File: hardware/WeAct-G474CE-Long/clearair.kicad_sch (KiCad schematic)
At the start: 36 parts, among them J1 220VAC mains in, M1 AC vent fan, M2 40mm fan (5V or 12V), Q1 2N7000, Q2 2N7000, Q3 2N2222A, Q4 IRFZ44N, SW1 RESET, SW2 COLD_BOOT, U1 SPS30, U2 BME680, U3 MQ131, U4 MiCS-4514, U5 RobotDyn AC dimmer

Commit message: encloser and buzzer
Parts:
- removed Q4: IRFZ44N, Package_TO_SOT_THT:TO-220-3_Vertical, symbol Transistor_FET:IRLZ44N
- removed R16: 10k, symbol Device:R
- added Q5: AO3400A, Package_TO_SOT_SMD:SOT-23, symbol Transistor_FET:AO3400A
- added R17: 100, symbol Device:R
- added R18: 100k, symbol Device:R
- added U6: PCF8563 RTC, libraries:PCF8563_HW689, symbol FullModules:PCF8563_HW689
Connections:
- net +3V3: now also U6.1 (VCC)
- net GND: now also U4.5 (PRE), Q5.2 (S), R18.2, U6.2 (GND); no longer U3.2 (GND)
- net at A.10 (PA15), R1.2, U1.3 (SCL)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: now also U6.4 (SCL)
- net at A.3 (PB7), R2.2, U1.2 (SDA)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: now also U6.3 (SDA)
- net at A.20 (PB12): now also R17.1; no longer U4.5 (PRE)
- net at Q3.3 (C): now also BZ1.2 (-)
- new net: Q5.1 (G), R17.2, R18.1
- new net: Q5.3 (D), U3.2 (GND)
- no-connect marks 53 -> 55
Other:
- note added: "Buzzer: PB15 (BUZZER_IN) -> R9 1k -> Q3 2N2222A base. Q3 switches the 12V buzzer on its low side: PB15 HIGH -> buzzer ON, LOW -> OFF. MiCS-4514 PRE tied to GND (boost not used). PB12 (MQ131_PREHEAT) -> R17 100R -> Q5 AO3400A gate, R18 100k pull-down: low-side switch in the MQ131 GND, HIGH = heater on. Cold/warm boot button SW2 -> PB14 (BOOT_MODE, pull-up). Gate PB1 (TRIAC_DIMMER) -> RobotDyn PSM."
- note added: "I2C1: PA15 SCL / PB7 SDA. SPS30 SEL=GND (I2C, 0x69); BME680 SDO=3V3 (0x77), CS=3V3; PCF8563 RTC HW-689 (0x51, CR1220, COT and INT unused). 4k7 pull-ups to 3V3."
- note removed: "Buzzer: PB15 (BUZZER_IN) -> R9 -> Q3. Q3 inverts: PB15 HIGH -> buzzer OFF; LOW -> R16 pulls IRFZ44N gate to 12V -> buzzer ON. MiCS-4514 PRE <- PB12 (MICS_PREHEAT). Cold/warm boot button SW2 -> PB14 (BOOT_MODE, pull-up). Gate PB1 (TRIAC_DIMMER) -> RobotDyn PSM."
- note removed: "I2C1: PA15 SCL / PB7 SDA. SPS30 SEL=GND (I2C, 0x69); BME680 SDO=3V3 (0x77), CS=3V3. 4k7 pull-ups to 3V3."

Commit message: try to make a pcb with 3D printer but the printer is dead.
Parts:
- removed JP1: FAN_V_SEL, symbol Jumper:Jumper_3_Open
- removed M2: 40mm fan (5V or 12V), symbol Motor:Fan
- removed Q5: AO3400A, Package_TO_SOT_SMD:SOT-23, symbol Transistor_FET:AO3400A
- removed R17: 100, symbol Device:R
- removed R18: 100k, symbol Device:R
- removed U1: SPS30, libraries:SPS30, symbol FullModules:SPS30
- removed U2: BME680, libraries:BME680_Board, symbol FullModules:BME680_Board
- removed U3: MQ131, libraries:MQ131_FlyingFish, symbol FullModules:MQ131_FlyingFish
- removed U4: MiCS-4514, libraries:MICS4514_Module, symbol FullModules:MICS4514_Module
- removed U6: PCF8563 RTC, libraries:PCF8563_HW689, symbol FullModules:PCF8563_HW689
- added J3: SPS30 wire header (1 VDD, 2 SDA, 3 SCL, 4 SEL, 5 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, Connector_PinHeader_2.54mm:PinHeader_1x05_P2.54mm_Vertical, symbol Connector_Generic:Conn_01x05
- added J4: BME680 wire header (1 VCC, 2 GND, 3 SCL, 4 SDA, 5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, Connector_PinHeader_2.54mm:PinHeader_1x06_P2.54mm_Vertical, symbol Connector_Generic:Conn_01x06
- added J5: MQ131 wire header (1 VCC, 2 GND, 3 DO nc, 4 AO), Connector_PinHeader_2.54mm:PinHeader_1x04_P2.54mm_Vertical, symbol Connector_Generic:Conn_01x04
- added J6: MiCS-4514 wire header (1 VCC, 2 GND, 3 RED, 4 NOX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, Connector_PinHeader_2.54mm:PinHeader_1x05_P2.54mm_Vertical, symbol Connector_Generic:Conn_01x05
- added J7: RTC PCF8563, Connector_PinHeader_2.54mm:PinHeader_1x04_P2.54mm_Vertical, symbol Connector_Generic:Conn_01x04
- added M2: 80mm fan front, Connector_PinHeader_2.54mm:PinHeader_1x04_P2.54mm_Vertical, symbol Connector_Generic:Conn_01x04
- added M3: 80mm fan rear, Connector_PinHeader_2.54mm:PinHeader_1x04_P2.54mm_Vertical, symbol Connector_Generic:Conn_01x04
- added R19, R20: 1k, Resistor_THT:R_Axial_DIN0207_L6.3mm_D2.5mm_P7.62mm_Horizontal, symbol Device:R
- added R21, R22: 10k, Resistor_THT:R_Axial_DIN0207_L6.3mm_D2.5mm_P7.62mm_Horizontal, symbol Device:R
- BZ1: footprint (none) -> Connector_PinHeader_2.54mm:PinHeader_1x02_P2.54mm_Vertical
- J1, M1: footprint (none) -> TerminalBlock_Phoenix:TerminalBlock_Phoenix_MKDS-1,5-2-5.08_1x02_P5.08mm_Horizontal
- J2: renamed from J; footprint (none) -> Connector_PinHeader_1.27mm:PinHeader_2x07_P1.27mm_Vertical
- PS1: value AC-DC PSU 220VAC -> 12V / 5V -> AC-DC PSUs 12V 2A + 5V 2A (DC out); footprint (none) -> libraries:PSU_DC_12V_5V_Inputs
- Q1, Q2, Q3: footprint Package_TO_SOT_THT:TO-92_Inline -> Package_TO_SOT_THT:TO-92_Inline_Wide
- R1, R10, R11, R12, R13, R14, R15, R2, R3, R4, R5, R6, R7, R8, R9: footprint (none) -> Resistor_THT:R_Axial_DIN0207_L6.3mm_D2.5mm_P7.62mm_Horizontal
- SW1, SW2: footprint (none) -> Button_Switch_THT:SW_PUSH_6mm
- U5: footprint (none) -> libraries:RobotDyn_Dimmer_Logic
- renumbered A to A1
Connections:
- net +12V: now also M2.2 (Pin_2), M3.2 (Pin_2)
- net +3V3: now also J4.1 (Pin_1), J4.5 (Pin_5), J4.6 (Pin_6), J7.1 (Pin_1), R21.1, R22.1
- net +5V: now also J3.1 (Pin_1), J5.1 (Pin_1), J6.1 (Pin_1)
- net GND: now also J3.4 (Pin_4), J3.5 (Pin_5), J4.2 (Pin_2), J5.2 (Pin_2), J6.2 (Pin_2), J6.5 (Pin_5), J7.2 (Pin_2), M2.1 (Pin_1), M3.1 (Pin_1)
- net at A1.10 (PA15), R1.2: now also J3.3 (Pin_3), J4.3 (Pin_3), J7.4 (Pin_4)
- net at A1.3 (PB7), R2.2: now also J3.2 (Pin_2), J4.4 (Pin_4), J7.3 (Pin_3)
- net at R7.1: now also J6.4 (Pin_4)
- net at R5.2: now also J6.3 (Pin_3)
- net at A1.14 (PA9): now also R20.2
- net at A1.15 (PA8): now also R19.2
- net at A1.30 (PA5): now also M2.3 (Pin_3), R21.2
- net at A1.7 (PB3): now also M3.3 (Pin_3), R22.2
- net at R3.1: now also J5.4 (Pin_4)
- new net: M3.4 (Pin_4), R20.1
- new net: M2.4 (Pin_4), R19.1
- no-connect marks 55 -> 50
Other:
- note added: "220VAC mains split: J1 -> RobotDyn TRIAC (fan) and two separate AC-DC supplies (12V 2A: buzzer + M2/M3 fans, 5V 2A: board + peripherals). Off board (on_board no): J1, M1 and the AC side of PS1 and U5, wired with 1.5 mm2 copper. The sensor modules (SPS30, BME680, MQ131, MiCS-4514) are off the PCB and are connected with wires to the PCB wire headers J3 (SPS30), J4 (BME680), J5 (MQ131) and J6 (MiCS-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"
- note added: "Buzzer: PB15 (BUZZER_IN) -> R9 1k -> Q3 2N2222A base. Q3 switches the 12V buzzer on its low side: PB15 HIGH -> buzzer ON, LOW -> OFF. MiCS-4514 PRE tied to GND (boost not used). MQ131 heater runs on a steady 5 V (VCC/GND straight to the rails, no switch); PB12 is unused. Cold/warm boot button SW2 -> PB14 (BOOT_MODE, pull-up). Gate PB1 (TRIAC_DIMMER) -> RobotDyn PSM."
- note added: "I2C1: PA15 SCL / PB7 SDA. SPS30 SEL=GND (I2C, 0x69); BME680 SDO=3V3 (0x77), CS=3V3; PCF8563 RTC HW-689 off-board on header J7 (VCC, GND, SDA, SCL; 0x51, CR1220, COT and INT unused). 4k7 pull-ups to 3V3."
- note removed: "220VAC mains split: J1 -> RobotDyn TRIAC (fan) and PS1 AC-DC (12V buzzer, 5V board + peripherals). PS1 pins: 1 L, 2 N, 3 +12V, 4 +5V, 5 GND. M2 40mm fan runs all the time. JP1: bridge 1-2 for a 5V fan, 2-3 for a 12V fan."
- note removed: "Buzzer: PB15 (BUZZER_IN) -> R9 1k -> Q3 2N2222A base. Q3 switches the 12V buzzer on its low side: PB15 HIGH -> buzzer ON, LOW -> OFF. MiCS-4514 PRE tied to GND (boost not used). PB12 (MQ131_PREHEAT) -> R17 100R -> Q5 AO3400A gate, R18 100k pull-down: low-side switch in the MQ131 GND, HIGH = heater on. Cold/warm boot button SW2 -> PB14 (BOOT_MODE, pull-up). Gate PB1 (TRIAC_DIMMER) -> RobotDyn PSM."
- note removed: "I2C1: PA15 SCL / PB7 SDA. SPS30 SEL=GND (I2C, 0x69); BME680 SDO=3V3 (0x77), CS=3V3; PCF8563 RTC HW-689 (0x51, CR1220, COT and INT unused). 4k7 pull-ups to 3V3."

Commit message: fix layout and script generators
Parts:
- J3: value SPS30 wire header (1 VDD, 2 SDA, 3 SCL, 4 SEL, 5 GND) -> SPS30
- J4: value BME680 wire header (1 VCC, 2 GND, 3 SCL, 4 SDA, 5 SDO, 6 CS) -> BME680
- J5: value MQ131 wire header (1 VCC, 2 GND, 3 DO nc, 4 AO) -> MQ131
- J6: value MiCS-4514 wire header (1 VCC, 2 GND, 3 RED, 4 NOX, 5 PRE) -> MiCS-4514
- SW1: value RESET -> RESET red; footprint Button_Switch_THT:SW_PUSH_6mm -> libraries:SW_Tactile_3x6_2pin
- SW2: value COLD_BOOT -> COLD_BOOT white; footprint Button_Switch_THT:SW_PUSH_6mm -> libraries:SW_Tactile_3x6_2pin
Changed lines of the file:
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@@
 			)
 		)
-		(property "Value" "MiCS-4514 wire header (1 VCC, 2 GND, 3 RED, 4 NOX, 5 PRE)"
+		(property "Value" "MiCS-4514"
 			(at 299.72 315.15 0)
 			(show_name no)
@@
 			)
 		)
-		(property "Description" "Wire header to the off-board sensor module"
+		(property "Description" "Wire header to the off-board sensor module Pins: 1 VCC, 2 GND, 3 RED, 4 NOX, 5 PRE"
 			(at 299.72 304.8 0)
 			(hide yes)
@@
 			)
 		)
-		(property "Value" "BME680 wire header (1 VCC, 2 GND, 3 SCL, 4 SDA, 5 SDO, 6 CS)"
+		(property "Value" "BME680"
 			(at 215.9 226.25 0)
 			(show_name no)
@@
 			)
 		)
-		(property "Description" "Wire header to the off-board sensor module"
+		(property "Description" "Wire header to the off-board sensor module Pins: 1 VCC, 2 GND, 3 SCL, 4 SDA, 5 SDO, 6 CS"
 			(at 215.9 214.63 0)
 			(hide yes)
@@
 			)
 		)
-		(property "Value" "COLD_BOOT"
+		(property "Value" "COLD_BOOT white"
 			(at 256.54 240.284 0)
 			(show_name no)
@@
 			)
 		)
-		(property "Footprint" "Button_Switch_THT:SW_PUSH_6mm"
+		(property "Footprint" "libraries:SW_Tactile_3x6_2pin"
 			(at 256.54 233.68 0)
 			(hide yes)
@@
 			)
 		)
-		(property "Description" "Push button switch, generic, two pins"
+		(property "Description" "Tactile push button 6 x 3.5 x 2.5 mm, 2 legs"
 			(at 256.54 238.76 0)
 			(hide yes)
@@
 			)
 		)
-		(property "Value" "RESET"
+		(property "Value" "RESET red"
 			(at 340.36 174.244 0)
 			(show_name no)
@@
 			)
 		)
-		(property "Footprint" "Button_Switch_THT:SW_PUSH_6mm"
+		(property "Footprint" "libraries:SW_Tactile_3x6_2pin"
 			(at 340.36 167.64 0)
 			(hide yes)
@@
 			)
 		)
-		(property "Description" "Push button switch, generic, two pins"
+		(property "Description" "Tactile push button 6 x 3.5 x 2.5 mm, 2 legs"
 			(at 340.36 172.72 0)
 			(hide yes)
@@
 			)
 		)
-		(property "Value" "SPS30 wire header (1 VDD, 2 SDA, 3 SCL, 4 SEL, 5 GND)"
+		(property "Value" "SPS30"
 			(at 215.9 190.69 0)
 			(show_name no)
@@
 			)
 		)
-		(property "Description" "Wire header to the off-board sensor module"
+		(property "Description" "Wire header to the off-board sensor module Pins: 1 VDD, 2 SDA, 3 SCL, 4 SEL, 5 GND"
 			(at 215.9 180.34 0)
 			(hide yes)
@@
 			)
 		)
-		(property "Value" "MQ131 wire header (1 VCC, 2 GND, 3 DO nc, 4 AO)"
+		(property "Value" "MQ131"
 			(at 396.24 189.42 0)
 			(show_name no)
@@
 			)
 		)
-		(property "Description" "Wire header to the off-board sensor module"
+		(property "Description" "Wire header to the off-board sensor module Pins: 1 VCC, 2 GND, 3 DO nc, 4 AO"
 			(at 396.24 180.34 0)
 			(hide yes)

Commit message: fix layout and script generators
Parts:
- A1: Net NRST (none) -> Reset button; Net PA0 (none) -> MQ131 out; Net PA1 (none) -> MiCS CO; Net PA15 (none) -> I2C SCL; Net PA5 (none) -> Front fan tach; Net PA7 (none) -> MiCS NO2; Net PA8 (none) -> Front fan PWM; Net PA9 (none) -> Rear fan PWM; Net PB0 (none) -> ZC in; Net PB1 (none) -> TRIAC gate; Net PB10 (none) -> Display TX; Net PB11 (none) -> Display RX; Net PB14 (none) -> Cold-boot button; Net PB15 (none) -> Buzzer drive; Net PB3 (none) -> Rear fan tach; Net PB7 (none) -> I2C SDA; Role (none) -> mcu female
- BZ1: Net - (none) -> Buzzer GND; Role (none) -> heavy
- J3: Role (none) -> sensor
- J5: Net Pin_4 (none) -> MQ131 out; Role (none) -> sensor
- J6: Net Pin_3 (none) -> MiCS CO; Net Pin_4 (none) -> MiCS NO2; Role (none) -> sensor
- M1: Role (none) -> heavy
- M2: Net Pin_4 (none) -> Front fan PWM; Role (none) -> heavy
- M3: Net Pin_4 (none) -> Rear fan PWM; Role (none) -> heavy
- PS1: Role (none) -> post heavy
- Q1: Net D (none) -> Display TX
- Q2: Net D (none) -> Display RX
- Q3: Net B (none) -> Buzzer base
- U5: Net Z-C (none) -> ZC out; Role (none) -> header

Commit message: crate a wire buses for power
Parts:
- R1, R2: Role (none) -> bus
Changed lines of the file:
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@@
+			)
+		)
+		(property "Role" "bus"
+			(at 248.92 144.78 0)
+			(hide yes)
+			(show_name no)
+			(do_not_autoplace no)
+			(effects
+				(font
+					(size 1.27 1.27)
+				)
 			)
 		)
@@
 			(at 259.08 144.78 0)
 			(hide yes)
+			(show_name no)
+			(do_not_autoplace no)
+			(effects
+				(font
+					(size 1.27 1.27)
+				)
+			)
+		)
+		(property "Role" "bus"
+			(at 259.08 144.78 0)
+			(hide yes)

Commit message: move buees on B1
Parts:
- R1, R2: Bus area (none) -> A14:Q18
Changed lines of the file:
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@@
+			)
+		)
+		(property "Bus area" "A14:Q18"
+			(at 248.92 144.78 0)
+			(hide yes)
+			(show_name no)
+			(do_not_autoplace no)
+			(effects
+				(font
+					(size 1.27 1.27)
+				)
 			)
 		)
@@
 			(at 259.08 144.78 0)
 			(hide yes)
+			(show_name no)
+			(do_not_autoplace no)
+			(effects
+				(font
+					(size 1.27 1.27)
+				)
+			)
+		)
+		(property "Bus area" "A14:Q18"
+			(at 259.08 144.78 0)
+			(hide yes)

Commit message: add optional wires
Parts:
- J7: Optional (none) -> RTC, planned
- Q1, Q2, R10, R11, R12, R13: Optional (none) -> Arduino display link, future
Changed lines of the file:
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@@
+			)
+		)
+		(property "Optional" "Arduino display link, future"
+			(at 406.4 205.74 0)
+			(hide yes)
+			(show_name no)
+			(do_not_autoplace no)
+			(effects
+				(font
+					(size 1.27 1.27)
+				)
 			)
 		)
@@
 			)
 		)
+		(property "Optional" "Arduino display link, future"
+			(at 419.1 243.84 0)
+			(hide yes)
+			(show_name no)
+			(do_not_autoplace no)
+			(effects
+				(font
+					(size 1.27 1.27)
+				)
+			)
+		)
 		(pin "1"
 		)
@@
 			)
 		)
+		(property "Optional" "Arduino display link, future"
+			(at 431.8 205.74 0)
+			(hide yes)
+			(show_name no)
+			(do_not_autoplace no)
+			(effects
+				(font
+					(size 1.27 1.27)
+				)
+			)
+		)
 		(pin "1"
 		)
@@
 			)
 		)
+		(property "Optional" "Arduino display link, future"
+			(at 406.4 233.68 0)
+			(hide yes)
+			(show_name no)
+			(do_not_autoplace no)
+			(effects
+				(font
+					(size 1.27 1.27)
+				)
+			)
+		)
 		(pin "1"
 		)
@@
 			)
 		)
+		(property "Optional" "Arduino display link, future"
+			(at 419.1 215.9 0)
+			(hide yes)
+			(show_name no)
+			(do_not_autoplace no)
+			(effects
+				(font
+					(size 1.27 1.27)
+				)
+			)
+		)
 		(pin "1"
 		)
@@
 			)
 		)
+		(property "Optional" "RTC, planned"
+			(at 238.76 195.58 0)
+			(hide yes)
+			(show_name no)
+			(do_not_autoplace no)
+			(effects
+				(font
+					(size 1.27 1.27)
+				)
+			)
+		)
 		(pin "1"
 		)
@@
 			(at 431.8 233.68 0)
 			(hide yes)
+			(show_name no)
+			(do_not_autoplace no)
+			(effects
+				(font
+					(size 1.27 1.27)
+				)
+			)
+		)
+		(property "Optional" "Arduino display link, future"
+			(at 431.8 233.68 0)
+			(hide yes)

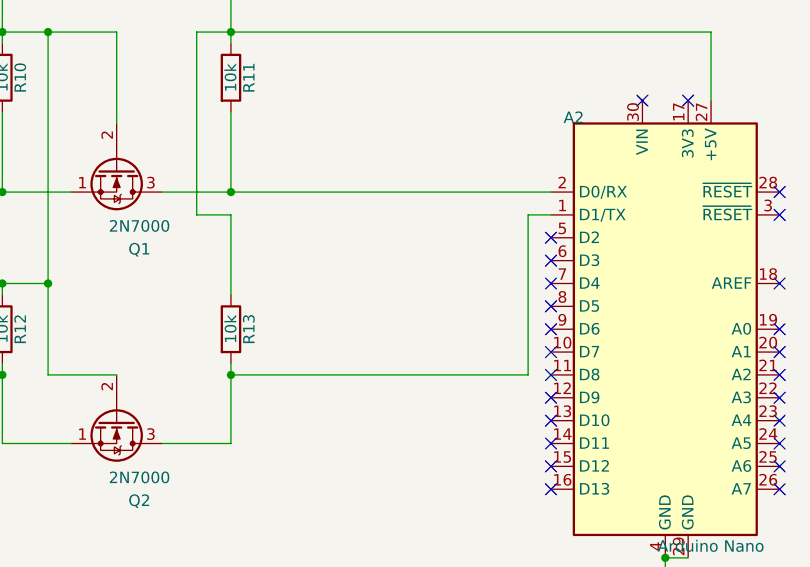
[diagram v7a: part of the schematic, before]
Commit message: add missing J8
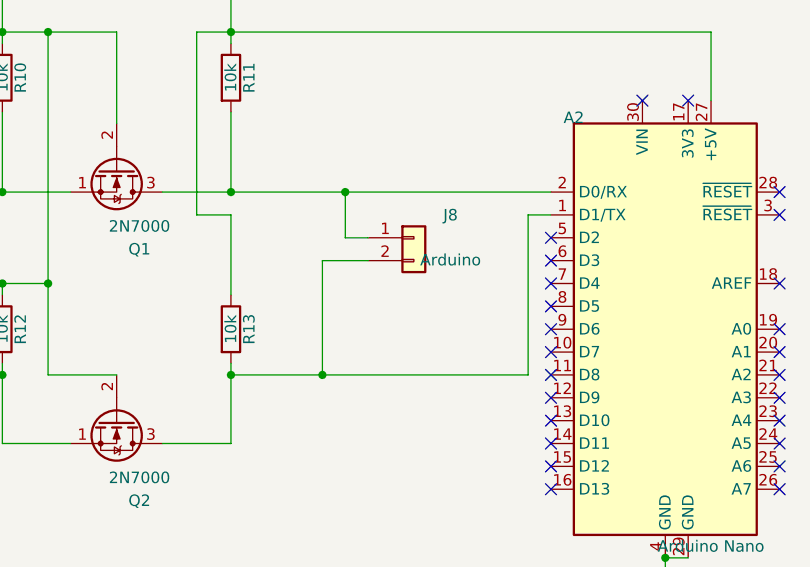
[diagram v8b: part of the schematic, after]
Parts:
- added J8: Arduino, Connector_PinHeader_2.54mm:PinHeader_1x02_P2.54mm_Vertical, symbol Connector_Generic:Conn_01x02
- J7: Optional RTC, planned -> (none)
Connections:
- net at A2.1 (D1/TX), Q2.3 (D), R13.2: now also J8.2 (Pin_2)
- net at A2.2 (D0/RX), Q1.3 (D), R11.2: now also J8.1 (Pin_1)
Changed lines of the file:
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@@
-			)
-		)
-		(property "Optional" "RTC, planned"
-			(at 238.76 195.58 0)
-			(hide yes)
-			(show_name no)
-			(do_not_autoplace no)
-			(effects
-				(font
-					(size 1.27 1.27)
-				)
 			)
 		)
@@
 	)
 	(symbol
+		(lib_id "Connector_Generic:Conn_01x02")
+		(at 452.12 223.52 0)
+		(unit 1)
+		(body_style 1)
+		(exclude_from_sim no)
+		(in_bom yes)
+		(on_board yes)
+		(in_pos_files yes)
+		(dnp no)
+		(property "Reference" "J8"
+			(at 456.2 221.0 0)
+			(show_name no)
+			(do_not_autoplace no)
+			(effects
+				(font
+					(size 1.27 1.27)
+				)
+			)
+		)
+		(property "Value" "Arduino"
+			(at 456.2 226.0 0)
+			(show_name no)
+			(do_not_autoplace no)
+			(effects
+				(font
+					(size 1.27 1.27)
+				)
+			)
+		)
+		(property "Footprint" "Connector_PinHeader_2.54mm:PinHeader_1x02_P2.54mm_Vertical"
+			(at 452.12 223.52 0)
+			(hide yes)
+			(show_name no)
+			(do_not_autoplace no)
+			(effects
+				(font
+					(size 1.27 1.27)
+				)
+			)
+		)
+		(property "Datasheet" ""
+			(at 452.12 223.52 0)
+			(hide yes)
+			(show_name no)
+			(do_not_autoplace no)
+			(effects
+				(font
+					(size 1.27 1.27)
+				)
+			)
+		)
+		(property "Description" "Header to the future Arduino display (Nano A2): 1 Display TX (to Arduino RX, 5V side of Q1), 2 Display RX (from Arduino TX, 5V side of Q2). The Arduino gets 5V and GND directly from the power supply."
+			(at 452.12 223.52 0)
+			(hide yes)
+			(show_name no)
+			(do_not_autoplace no)
+			(effects
+				(font
+					(size 1.27 1.27)
+				)
+			)
+		)
+		(pin "1"
+		)
+		(pin "2"
+		)
+		(instances
+			(project "clearair"
+				(path "/953560a5-36cf-5251-8f8d-509802d70a69"
+					(reference "J8")
+					(unit 1)
+				)
+			)
+		)
+	)
+	(wire
+		(pts
+			(xy 447.04 223.52) (xy 444.5 223.52)
+		)
+		(stroke
+			(width 0)
+			(type default)
+		)
+	)
+	(wire
+		(pts
+			(xy 444.5 223.52) (xy 444.5 218.44)
+		)
+		(stroke
+			(width 0)
+			(type default)
+		)
+	)
+	(junction
+		(at 444.5 218.44)
+		(diameter 0)
+		(color 0 0 0 0)
+	)
+	(wire
+		(pts
+			(xy 447.04 226.06) (xy 441.96 226.06)
+		)
+		(stroke
+			(width 0)
+			(type default)
+		)
+	)
+	(wire
+		(pts
+			(xy 441.96 226.06) (xy 441.96 238.76)
+		)
+		(stroke
+			(width 0)
+			(type default)
+		)
+	)
+	(junction
+		(at 441.96 238.76)
+		(diameter 0)
+		(color 0 0 0 0)
+	)
+	(symbol
